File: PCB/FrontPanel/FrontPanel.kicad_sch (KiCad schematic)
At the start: 52 parts, among them J1 Conn_01x05, J2 Conn_01x03, Q1 2N7002, Q2 2N7002, Q3 2N7002, Q4 2N7002, Q5 2N7002, SW1 SW_SPDT, SW10 RArrow, SW2 RotaryEncoder_Switch, SW3 IndepChSelect, SW4 SeriesChSelect, SW5 ParChSelect, SW6 ChAEnable, SW7 ChBEnable, SW8 ABSelect, SW9 LArrow, U1 MCU_ST_STM32G0:STM32G031F6Px, U2 CD74HC4067SM

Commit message: Add SWD connector
USART programming is fraught with problems. It's much much
better to use SWD through an STDC14 connector.
Increased version number to v1.3
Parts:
- removed J2: Conn_01x03, Connector_PinHeader_2.54mm:PinHeader_1x03_P2.54mm_Vertical, symbol Connector_Generic:Conn_01x03
- removed SW1: SW_SPDT, Footprints:Switch_SPDT_P2.54mm, symbol Switch:SW_SPDT
- added J2: SWD, Connector_PinHeader_1.27mm:PinHeader_2x07_P1.27mm_Vertical_SMD, symbol Connector:Conn_ST_STDC14
- C1: JLC 0805 -> (none)
- renumbered R13 to R11, R14 to R12, R15 to R13, R16 to R14, R17 to R15, R11 to R16, R12 to R17, SW2 to SW1, SW3 to SW2, SW4 to SW3, SW5 to SW4, SW6 to SW5, SW7 to SW6, SW8 to SW7, SW9 to SW8, SW10 to SW9
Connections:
- net GND: now also J2.5 (GND), J2.7 (GND)
- net NRESET: now also J2.12 (~{RST})
- net UART_RX: now also J2.14 (VCP_TX)
- net UART_TX: now also J2.13 (VCP_RX)
- net VCC: now also J2.3 (VCC)
- net BOOT0 renamed SWCLK
- net SWCLK: now also J2.6 (JCLK/SWCLK)
- net S1 renamed SWDIO/S1
- net SWDIO/S1: now also J2.4 (JTMS/SWDIO)
- no-connect marks 0 -> 4
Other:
- moved on the sheet: H1, H2, H3, H4, R16, R17, SW1

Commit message: Give names to all networks a name
Add network labels to networks that didn't yet have a name.
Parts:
- C1: value (none) -> 100nF; footprint (none) -> Capacitor_SMD:C_0805_2012Metric_Pad1.18x1.45mm_HandSolder
- C2: value (none) -> 4.7uF; footprint (none) -> Capacitor_SMD:C_0805_2012Metric_Pad1.18x1.45mm_HandSolder
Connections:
- net ChBEnableSw: now reaches R14.1, SW6.1 (A), U2.17 (I14)
- net SeriesSelectSw: now reaches R18.1, SW3.1 (A), U2.6 (I3)
- net IndepSelectSw: now reaches R13.1, SW2.1 (A), U2.3 (I6)
- net LArrowSw: now reaches R12.1, SW8.1 (A), U2.2 (I7)
- net ParSelectSw: now reaches R19.1, SW4.1 (A), U2.7 (I2)
- net RArrowSw: now reaches R11.1, SW9.1 (A), U2.23 (I8)
- net ChAEnableSw: now reaches R15.1, SW5.1 (A), U2.16 (I15)
- net ABSelectSw: now reaches R20.1, SW7.1 (A), U2.8 (I1)
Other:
- title: (none) -> Front del Gat Front Panel
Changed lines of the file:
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@@
 (kicad_sch (version 20211123) (generator eeschema)
   (paper "A4")
+  (title_block
+    (title "Front del Gat Front Panel")
+    (date "2022-09-25")
+    (rev "1.3")
+  )
   (junction (at 232.41 36.83) (diameter 1.016) (color 0 0 0 0)
   )
@@
   (wire (pts (xy 214.63 102.87) (xy 238.76 102.87))
     (stroke (width 0) (type default) (color 0 0 0 0))
+  )
+  (label "LArrowSw" (at 203.2 129.54 90)
+    (effects (font (size 1.27 1.27)) (justify left bottom))
+  )
+  (label "ChBEnableSw" (at 213.36 129.54 90)
+    (effects (font (size 1.27 1.27)) (justify left bottom))
+  )
+  (label "IndepSelectSw" (at 208.28 129.54 90)
+    (effects (font (size 1.27 1.27)) (justify left bottom))
+  )
+  (label "ChAEnableSw" (at 218.44 129.54 90)
+    (effects (font (size 1.27 1.27)) (justify left bottom))
+  )
+  (label "ParSelectSw" (at 228.6 129.54 90)
+    (effects (font (size 1.27 1.27)) (justify left bottom))
+  )
+  (label "ABSelectSw" (at 233.68 129.54 90)
+    (effects (font (size 1.27 1.27)) (justify left bottom))
+  )
+  (label "RArrowSw" (at 198.12 129.54 90)
+    (effects (font (size 1.27 1.27)) (justify left bottom))
+  )
+  (label "SeriesSelectSw" (at 223.52 129.54 90)
+    (effects (font (size 1.27 1.27)) (justify left bottom))
+  )
+  (label "EncoderSw" (at 238.76 129.54 90)
+    (effects (font (size 1.27 1.27)) (justify left bottom))
   )
   (global_label "PAR_CHANNEL_EN" (shape input) (at 33.02 115.57 180)
@@
       (effects (font (size 1.27 1.27)) (justify left))
     )
-    (property "Value" "" (id 1) (at 115.57 146.0499 0)
-      (effects (font (size 1.27 1.27)) (justify left))
-    )
-    (property "Footprint" "" (id 2) (at 112.7252 148.59 0)
+    (property "Value" "4.7uF" (id 1) (at 115.57 146.0499 0)
+      (effects (font (size 1.27 1.27)) (justify left))
+    )
+    (property "Footprint" "Capacitor_SMD:C_0805_2012Metric_Pad1.18x1.45mm_HandSolder" (id 2) (at 112.7252 148.59 0)
       (effects (font (size 1.27 1.27)) hide)
     )
@@
       (effects (font (size 1.27 1.27)) (justify left))
     )
-    (property "Value" "" (id 1) (at 95.25 146.05 0)
-      (effects (font (size 1.27 1.27)) (justify left))
-    )
-    (property "Footprint" "" (id 2) (at 105.1052 148.59 0)
-      (effects (font (size 1.27 1.27)) hide)
-    )
+    (property "Value" "100nF" (id 1) (at 95.25 146.05 0)
+      (effects (font (size 1.27 1.27)) (justify left))
+    )
+    (property "Footprint" "Capacitor_SMD:C_0805_2012Metric_Pad1.18x1.45mm_HandSolder" (id 2) (at 105.1052 148.59 0)
+      (effects (font (size 1.27 1.27)) hide)
+    )

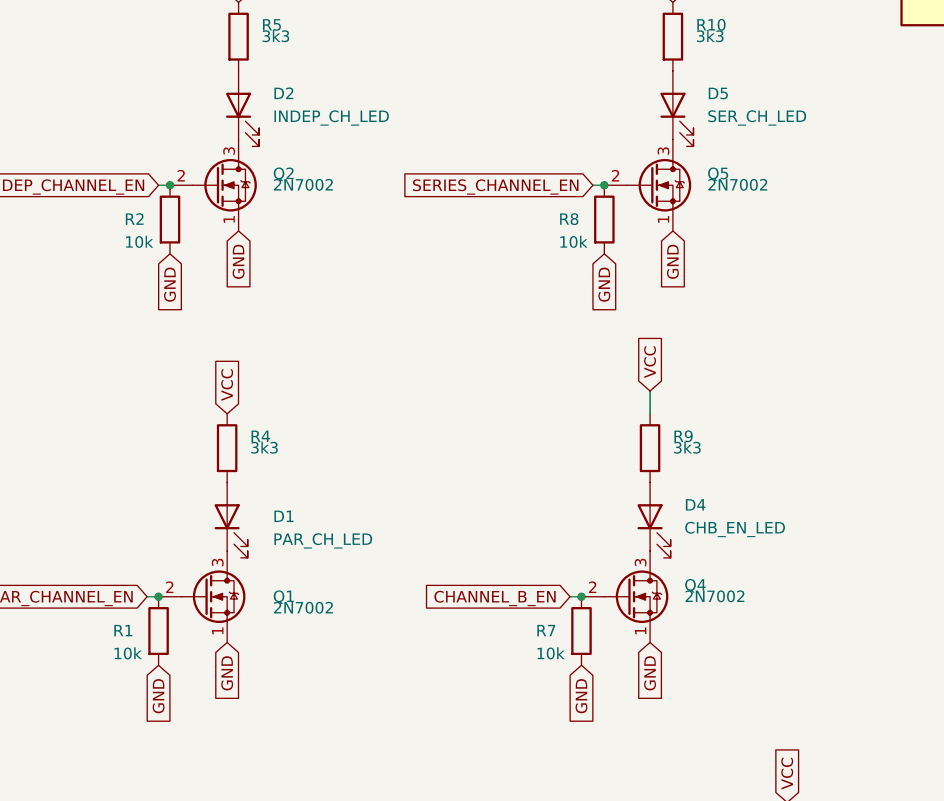
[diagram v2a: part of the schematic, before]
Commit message: Fix 2N7002 footprint
The footprint for the 2N7002 MOSFETs was taken from the one
of a 2N7000, which has the gate and the source pins exchanged.
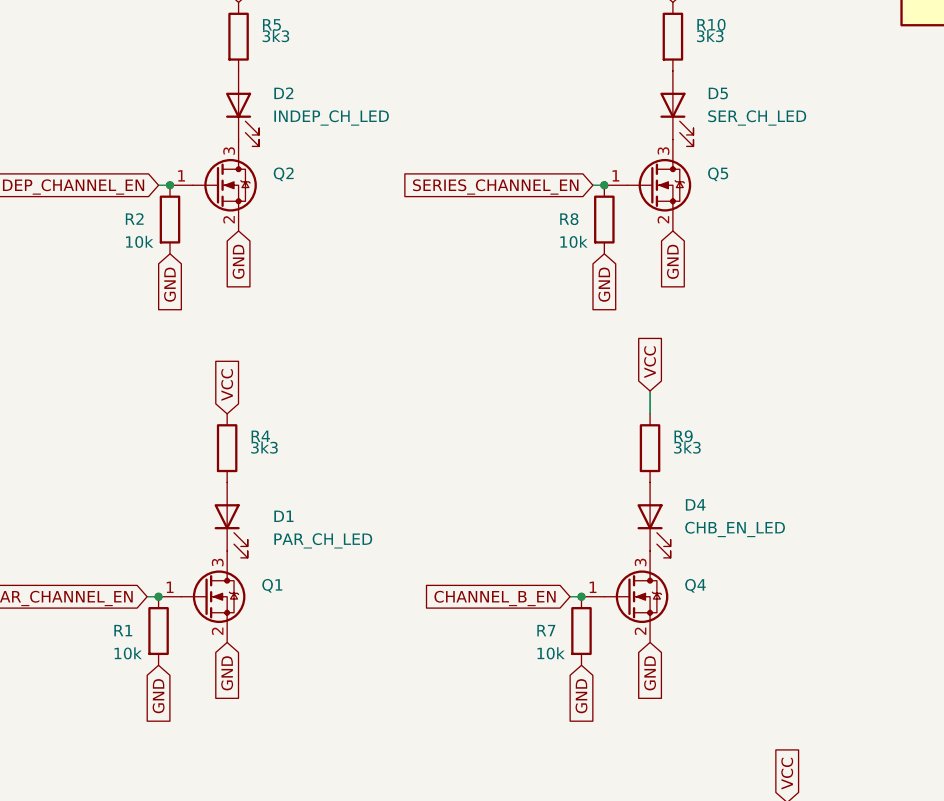
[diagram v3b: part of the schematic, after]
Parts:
- removed Q1, Q2, Q4, Q5: 2N7002, Package_TO_SOT_SMD:SOT-23, symbol Transistor_FET:2N7000
- added Q1, Q2, Q4, Q5: (no value), symbol Transistor_FET:2N7002
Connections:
- net CHANNEL_B_EN: now also Q4.1 (G)
- net GND: now also Q1.2 (S), Q2.2 (S), Q4.2 (S), Q5.2 (S)
- net INDEP_CHANNEL_EN: now also Q2.1 (G)
- net PAR_CHANNEL_EN: now also Q1.1 (G)
- net SERIES_CHANNEL_EN: now also Q5.1 (G)
- net at D2.1 (K): now also Q2.3 (D)
- net at D4.1 (K): now also Q4.3 (D)
- net at D1.1 (K): now also Q1.3 (D)
- net at D5.1 (K): now also Q5.3 (D)
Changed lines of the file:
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@@
   (junction (at 262.89 85.09) (diameter 1.016) (color 0 0 0 0)
   )
+  (junction (at 83.82 69.85) (diameter 0) (color 0 0 0 0)
+  )
   (junction (at 262.89 114.3) (diameter 0) (color 0 0 0 0)
   )
@@
   (junction (at 223.52 85.09) (diameter 0) (color 0 0 0 0)
   )
+  (junction (at 35.56 69.85) (diameter 0) (color 0 0 0 0)
+  )
   (junction (at 262.89 105.41) (diameter 0) (color 0 0 0 0)
   )
@@
   (junction (at 210.82 36.83) (diameter 1.016) (color 0 0 0 0)
   )
-  (junction (at 35.56 69.85) (diameter 0) (color 0 0 0 0)
-  )
   (junction (at 262.89 77.47) (diameter 0) (color 0 0 0 0)
   )
+  (junction (at 262.89 95.25) (diameter 1.016) (color 0 0 0 0)
+  )
+  (junction (at 34.29 115.57) (diameter 0) (color 0 0 0 0)
+  )
   (junction (at 81.28 115.57) (diameter 0) (color 0 0 0 0)
-  )
-  (junction (at 262.89 95.25) (diameter 1.016) (color 0 0 0 0)
-  )
-  (junction (at 83.82 69.85) (diameter 0) (color 0 0 0 0)
-  )
-  (junction (at 34.29 115.57) (diameter 0) (color 0 0 0 0)
   )
   (junction (at 40.64 26.67) (diameter 0) (color 0 0 0 0)
@@
     (pin "2")
   )
+  (symbol (lib_id "Transistor_FET:2N7002") (at 88.9 69.85 0) (unit 1)
+    (in_bom yes) (on_board yes) (fields_autoplaced)
+    (property "Reference" "Q5" (id 0) (at 95.25 68.5799 0)
+      (effects (font (size 1.27 1.27)) (justify left))
+    )
+    (property "Value" "" (id 1) (at 95.25 71.1199 0)
+      (effects (font (size 1.27 1.27)) (justify left))
+    )
+    (property "Footprint" "" (id 2) (at 93.98 71.755 0)
+      (effects (font (size 1.27 1.27) italic) (justify left) hide)
+    )
+    (property "Datasheet" "https://www.onsemi.com/pub/Collateral/NDS7002A-D.PDF" (id 3) (at 88.9 69.85 0)
+      (effects (font (size 1.27 1.27)) (justify left) hide)
+    )
+    (pin "1")
+    (pin "2")
+    (pin "3")
+  )
   (symbol (lib_id "power:GND") (at 128.27 166.37 0) (unit 1)
     (in_bom yes) (on_board yes) (fields_autoplaced)
@@
     (pin "3")
   )
-  (symbol (lib_id "Transistor_FET:2N7000") (at 40.64 69.85 0) (unit 1)
-    (in_bom yes) (on_board yes)
-    (property "Reference" "Q2" (id 0) (at 46.99 68.58 0)
-      (effects (font (size 1.27 1.27)) (justify left))
-    )
-    (property "Value" "2N7002" (id 1) (at 46.99 69.85 0)
-      (effects (font (size 1.27 1.27)) (justify left))
-    )
-    (property "Footprint" "Package_TO_SOT_SMD:SOT-23" (id 2) (at 45.72 71.755 0)
-      (effects (font (size 1.27 1.27) italic) (justify left) hide)
-    )
-    (property "Datasheet" "https://www.onsemi.com/pub/Collateral/NDS7002A-D.PDF" (id 3) (at 40.64 69.85 0)
-      (effects (font (size 1.27 1.27)) (justify left) hide)
-    )
-    (pin "1")
-    (pin "2")
-    (pin "3")
-  )
   (symbol (lib_id "Device:R") (at 40.64 172.72 0) (unit 1)
     (in_bom yes) (on_board yes)
@@
     (pin "2")
   )
-  (symbol (lib_id "Transistor_FET:2N7000") (at 86.36 115.57 0) (unit 1)
-    (in_bom yes) (on_board yes)
-    (property "Reference" "Q4" (id 0) (at 92.71 114.3 0)
-      (effects (font (size 1.27 1.27)) (justify left))
-    )
-    (property "Value" "2N7002" (id 1) (at 92.71 115.57 0)
-      (effects (font (size 1.27 1.27)) (justify left))
-    )
-    (property "Footprint" "Package_TO_SOT_SMD:SOT-23" (id 2) (at 91.44 117.475 0)
-      (effects (font (size 1.27 1.27) italic) (justify left) hide)
-    )
-    (property "Datasheet" "https://www.onsemi.com/pub/Collateral/NDS7002A-D.PDF" (id 3) (at 86.36 115.57 0)
-      (effects (font (size 1.27 1.27)) (justify left) hide)
-    )
-    (pin "1")
-    (pin "2")
-    (pin "3")
-  )
   (symbol (lib_id "power:GND") (at 80.01 184.15 0) (unit 1)
     (in_bom yes) (on_board yes) (fields_autoplaced)
@@
     )
     (pin "1")
-  )
-  (symbol (lib_id "Transistor_FET:2N7000") (at 39.37 115.57 0) (unit 1)
-    (in_bom yes) (on_board yes)
-    (property "Reference" "Q1" (id 0) (at 46.99 115.57 0)
-      (effects (font (size 1.27 1.27)) (justify left))
-    )
-    (property "Value" "2N7002" (id 1) (at 46.99 116.84 0)
-      (effects (font (size 1.27 1.27)) (justify left))
-    )
-    (property "Footprint" "Package_TO_SOT_SMD:SOT-23" (id 2) (at 44.45 117.475 0)
-      (effects (font (size 1.27 1.27) italic) (justify left) hide)
-    )
-    (property "Datasheet" "https://www.onsemi.com/pub/Collateral/NDS7002A-D.PDF" (id 3) (at 39.37 115.57 0)
-      (effects (font (size 1.27 1.27)) (justify left) hide)
-    )
-    (pin "1")
-    (pin "2")
-    (pin "3")
   )
   (symbol (lib_id "Device:R") (at 222.25 41.91 90) (unit 1)
@@
     (pin "2")
   )
+  (symbol (lib_id "Transistor_FET:2N7002") (at 40.64 69.85 0) (unit 1)
+    (in_bom yes) (on_board yes) (fields_autoplaced)
+    (property "Reference" "Q2" (id 0) (at 46.99 68.5799 0)
+      (effects (font (size 1.27 1.27)) (justify left))
+    )
+    (property "Value" "" (id 1) (at 46.99 71.1199 0)
+      (effects (font (size 1.27 1.27)) (justify left))
+    )
+    (property "Footprint" "" (id 2) (at 45.72 71.755 0)
+      (effects (font (size 1.27 1.27) italic) (justify left) hide)
+    )
+    (property "Datasheet" "https://www.onsemi.com/pub/Collateral/NDS7002A-D.PDF" (id 3) (at 40.64 69.85 0)
+      (effects (font (size 1.27 1.27)) (justify left) hide)
+    )
+    (pin "1")
+    (pin "2")
+    (pin "3")
+  )
   (symbol (lib_id "Switch:SW_SPST") (at 250.19 140.97 0) (unit 1)
     (in_bom yes) (on_board yes)
@@
     (pin "2")
   )
-  (symbol (lib_id "Transistor_FET:2N7000") (at 88.9 69.85 0) (unit 1)
-    (in_bom yes) (on_board yes)
-    (property "Reference" "Q5" (id 0) (at 95.25 68.58 0)
-      (effects (font (size 1.27 1.27)) (justify left))
-    )
-    (property "Value" "2N7002" (id 1) (at 95.25 69.85 0)
-      (effects (font (size 1.27 1.27)) (justify left))
-    )
-    (property "Footprint" "Package_TO_SOT_SMD:SOT-23" (id 2) (at 93.98 71.755 0)
-      (effects (font (size 1.27 1.27) italic) (justify left) hide)
-    )
-    (property "Datasheet" "https://www.onsemi.com/pub/Collateral/NDS7002A-D.PDF" (id 3) (at 88.9 69.85 0)
-      (effects (font (size 1.27 1.27)) (justify left) hide)
-    )
-    (pin "1")
-    (pin "2")
-    (pin "3")
-  )
   (symbol (lib_id "power:GND") (at 138.43 190.5 0) (unit 1)
     (in_bom yes) (on_board yes) (fields_autoplaced)
@@
     (pin "2")
   )
+  (symbol (lib_id "Transistor_FET:2N7002") (at 86.36 115.57 0) (unit 1)
+    (in_bom yes) (on_board yes) (fields_autoplaced)
+    (property "Reference" "Q4" (id 0) (at 92.71 114.2999 0)
+      (effects (font (size 1.27 1.27)) (justify left))
+    )
+    (property "Value" "" (id 1) (at 92.71 116.8399 0)
+      (effects (font (size 1.27 1.27)) (justify left))
+    )
+    (property "Footprint" "" (id 2) (at 91.44 117.475 0)
+      (effects (font (size 1.27 1.27) italic) (justify left) hide)
+    )
+    (property "Datasheet" "https://www.onsemi.com/pub/Collateral/NDS7002A-D.PDF" (id 3) (at 86.36 115.57 0)
+      (effects (font (size 1.27 1.27)) (justify left) hide)
+    )
+    (pin "1")
+    (pin "2")
+    (pin "3")
+  )
   (symbol (lib_id "power:PWR_FLAG") (at 40.64 26.67 0) (unit 1)
     (in_bom yes) (on_board yes) (fields_autoplaced)
@@
     (pin "1")
     (pin "2")
+  )
+  (symbol (lib_id "Transistor_FET:2N7002") (at 39.37 115.57 0) (unit 1)
+    (in_bom yes) (on_board yes) (fields_autoplaced)
+    (property "Reference" "Q1" (id 0) (at 45.72 114.2999 0)
+      (effects (font (size 1.27 1.27)) (justify left))
+    )
+    (property "Value" "" (id 1) (at 45.72 116.8399 0)
+      (effects (font (size 1.27 1.27)) (justify left))
+    )
+    (property "Footprint" "" (id 2) (at 44.45 117.475 0)
+      (effects (font (size 1.27 1.27) italic) (justify left) hide)
+    )
+    (property "Datasheet" "https://www.onsemi.com/pub/Collateral/NDS7002A-D.PDF" (id 3) (at 39.37 115.57 0)
+      (effects (font (size 1.27 1.27)) (justify left) hide)
+    )
+    (pin "1")
+    (pin "2")
+    (pin "3")
   )
   (symbol (lib_id "Device:C") (at 104.14 144.78 0) (unit 1)
@@
       (reference "J2") (unit 1) (value "SWD") (footprint "Connector_PinHeader_1.27mm:PinHeader_2x07_P1.27mm_Vertical_SMD")
     )
-    (path "/8710c6a4-cf4d-4843-b886-27e943825c0b"
+    (path "/f5bb5187-3318-4d46-8623-181db05b6fc2"
       (reference "Q1") (unit 1) (value "2N7002") (footprint "Package_TO_SOT_SMD:SOT-23")
     )
-    (path "/458a2900-02b5-43f1-9744-a955ef4e3558"
+    (path "/c3f23d07-a72a-42cc-a576-aacd2bbb7961"
       (reference "Q2") (unit 1) (value "2N7002") (footprint "Package_TO_SOT_SMD:SOT-23")
     )
@@
       (reference "Q3") (unit 1) (value "2N7002") (footprint "Package_TO_SOT_SMD:SOT-23")
     )
-    (path "/7b79dcdd-2456-415a-9e97-6e65356be301"
+    (path "/e34bd42a-4eff-4f71-8c2d-bab0b02ba0d3"
       (reference "Q4") (unit 1) (value "2N7002") (footprint "Package_TO_SOT_SMD:SOT-23")
     )
-    (path "/d19511b2-5790-4240-a34e-353a5ea87d21"
+    (path "/16c8b92f-96de-43c6-befb-6bfee5b95fc6"
       (reference "Q5") (unit 1) (value "2N7002") (footprint "Package_TO_SOT_SMD:SOT-23")
     )
